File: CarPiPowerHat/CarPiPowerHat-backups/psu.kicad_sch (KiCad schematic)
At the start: 43 parts, among them IC1 AP2331TDSA-7, J10 Conn_01x02_Male, J5 USB_A, Q1 DMMT5401, Q2 DMG2305UX, Q3 DMP3013SFV-7, U1 AP64501SP-13

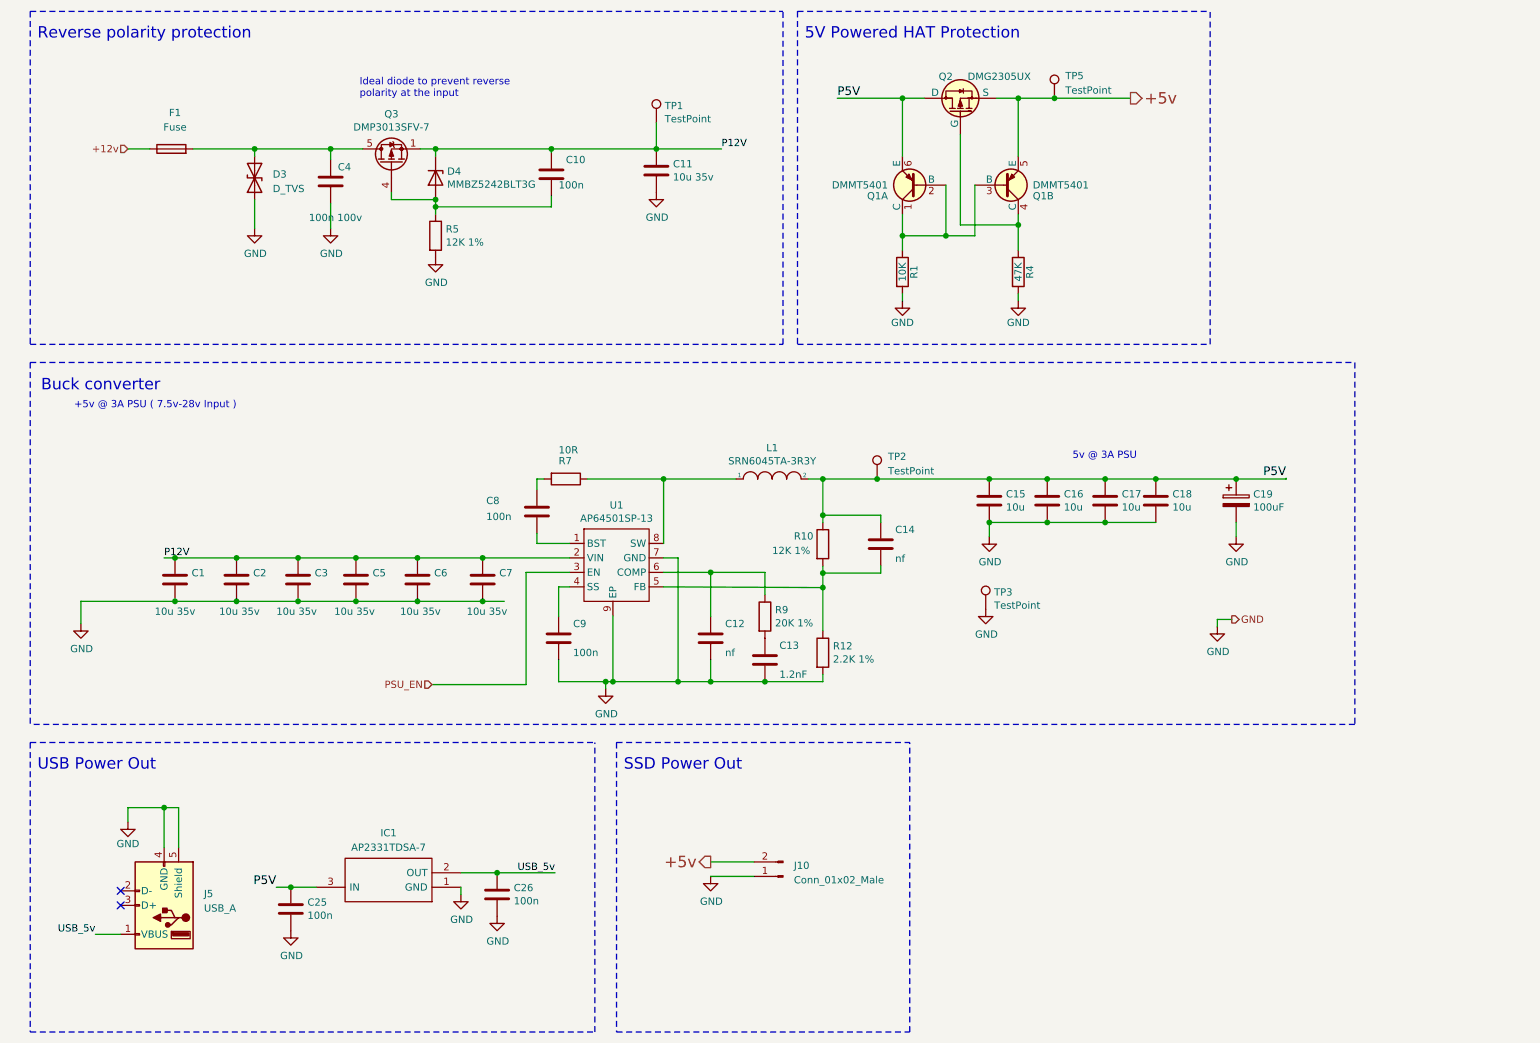
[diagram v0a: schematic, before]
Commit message: Repositioning of connectors
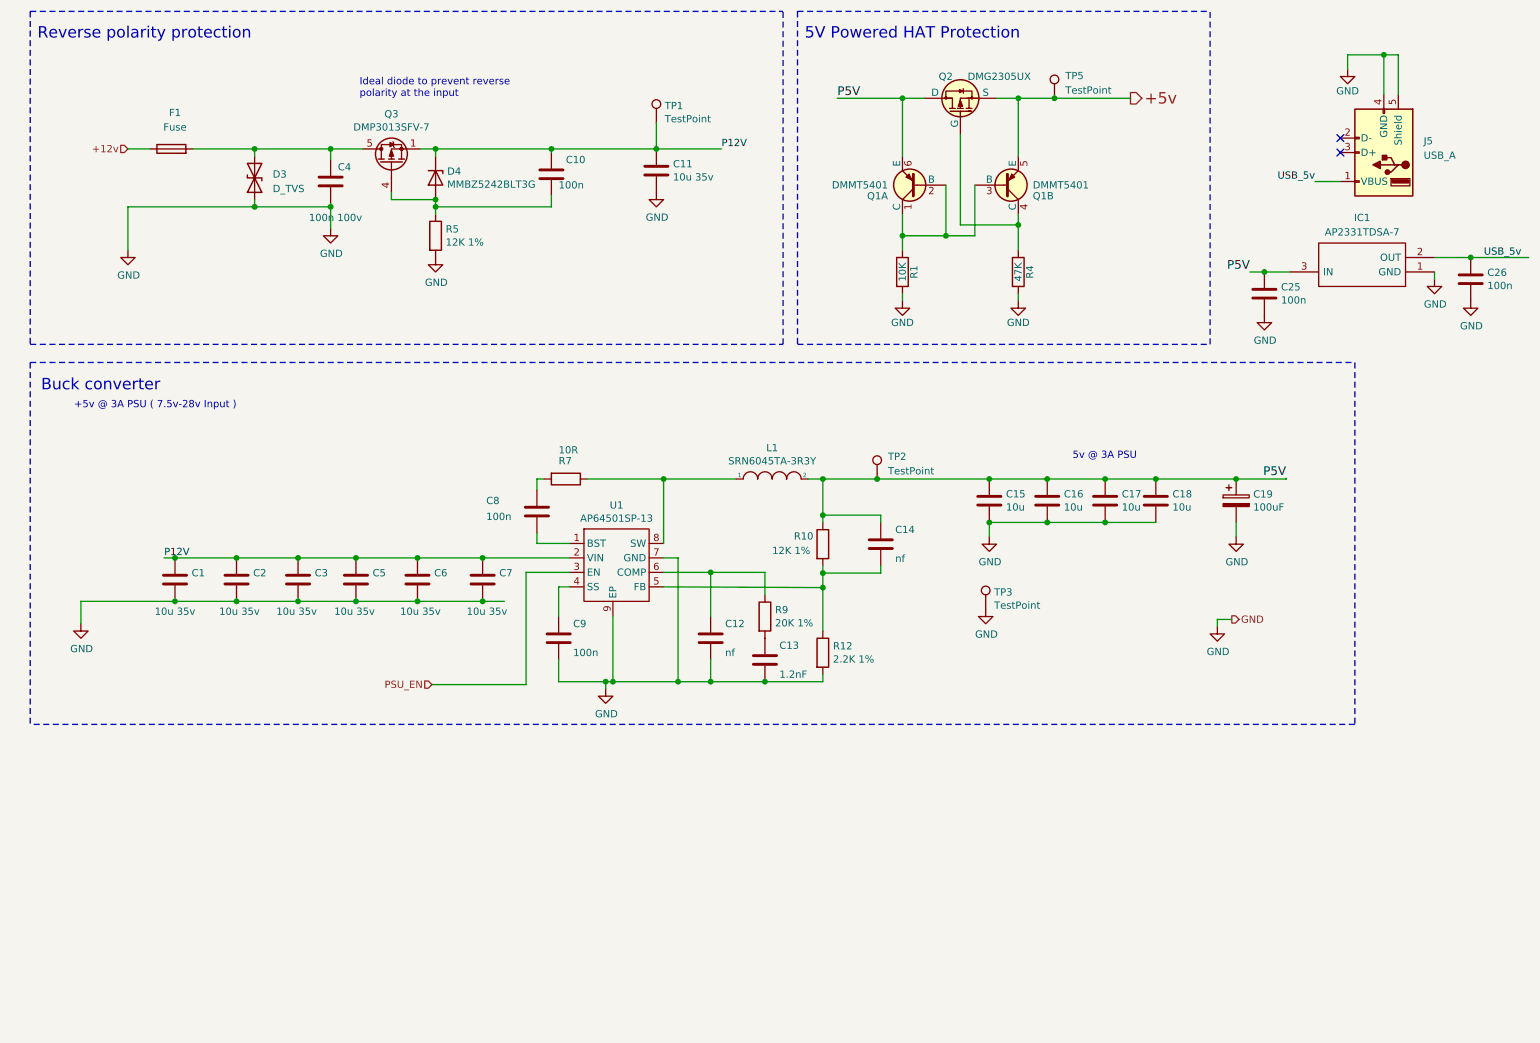
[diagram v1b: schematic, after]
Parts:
- removed J10: Conn_01x02_Male, Connector_JST:JST_XH_S2B-XH-A_1x02_P2.50mm_Horizontal, symbol Connector:Conn_01x02_Male
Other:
- note removed: "SSD Power Out"
- note removed: "USB Power Out"
- moved on the sheet: C25, C26, IC1, J5
